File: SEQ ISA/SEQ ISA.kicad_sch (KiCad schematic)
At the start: 70 parts, among them IC1 TLX9310_TPL,F, IC2 SN74LVC4245ADW, J1 FTSH-107-01-L-DV-K-A, J2 Conn_01x02_Pin, J3 Conn_01x02_Pin, J4 Conn_01x02_Pin, J5 Conn_01x02_Pin, J6 Conn_01x02_Pin, J7 Jack-DC, J8 Conn_01x04_Pin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

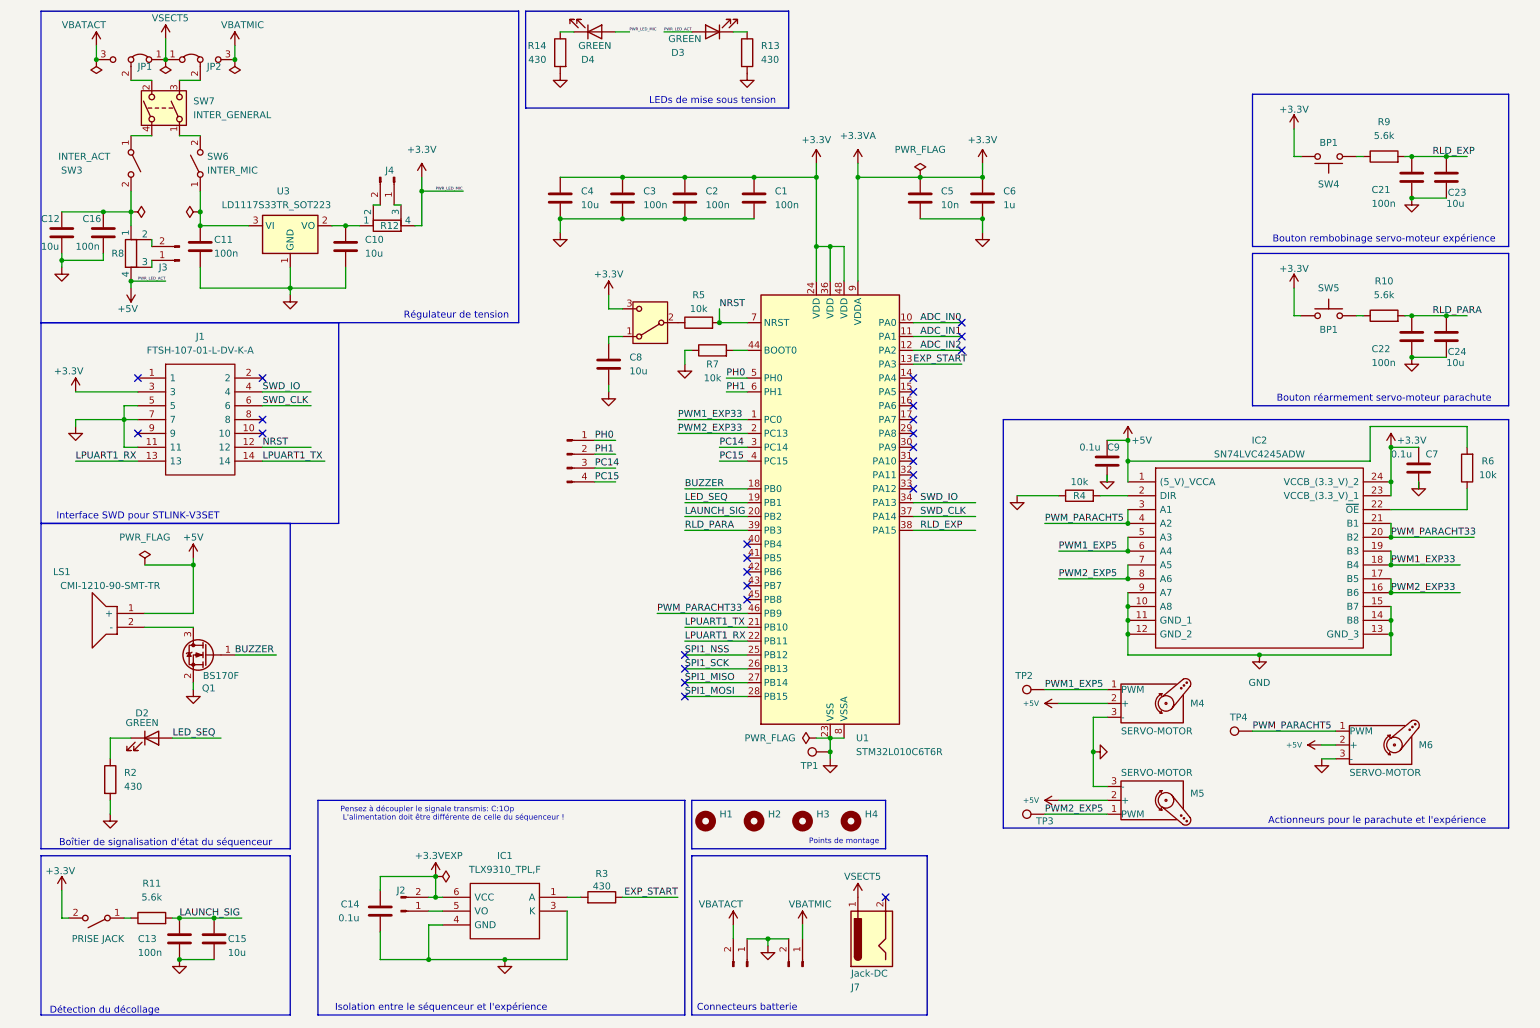
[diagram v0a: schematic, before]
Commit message: Update to KicadV9 + C movement
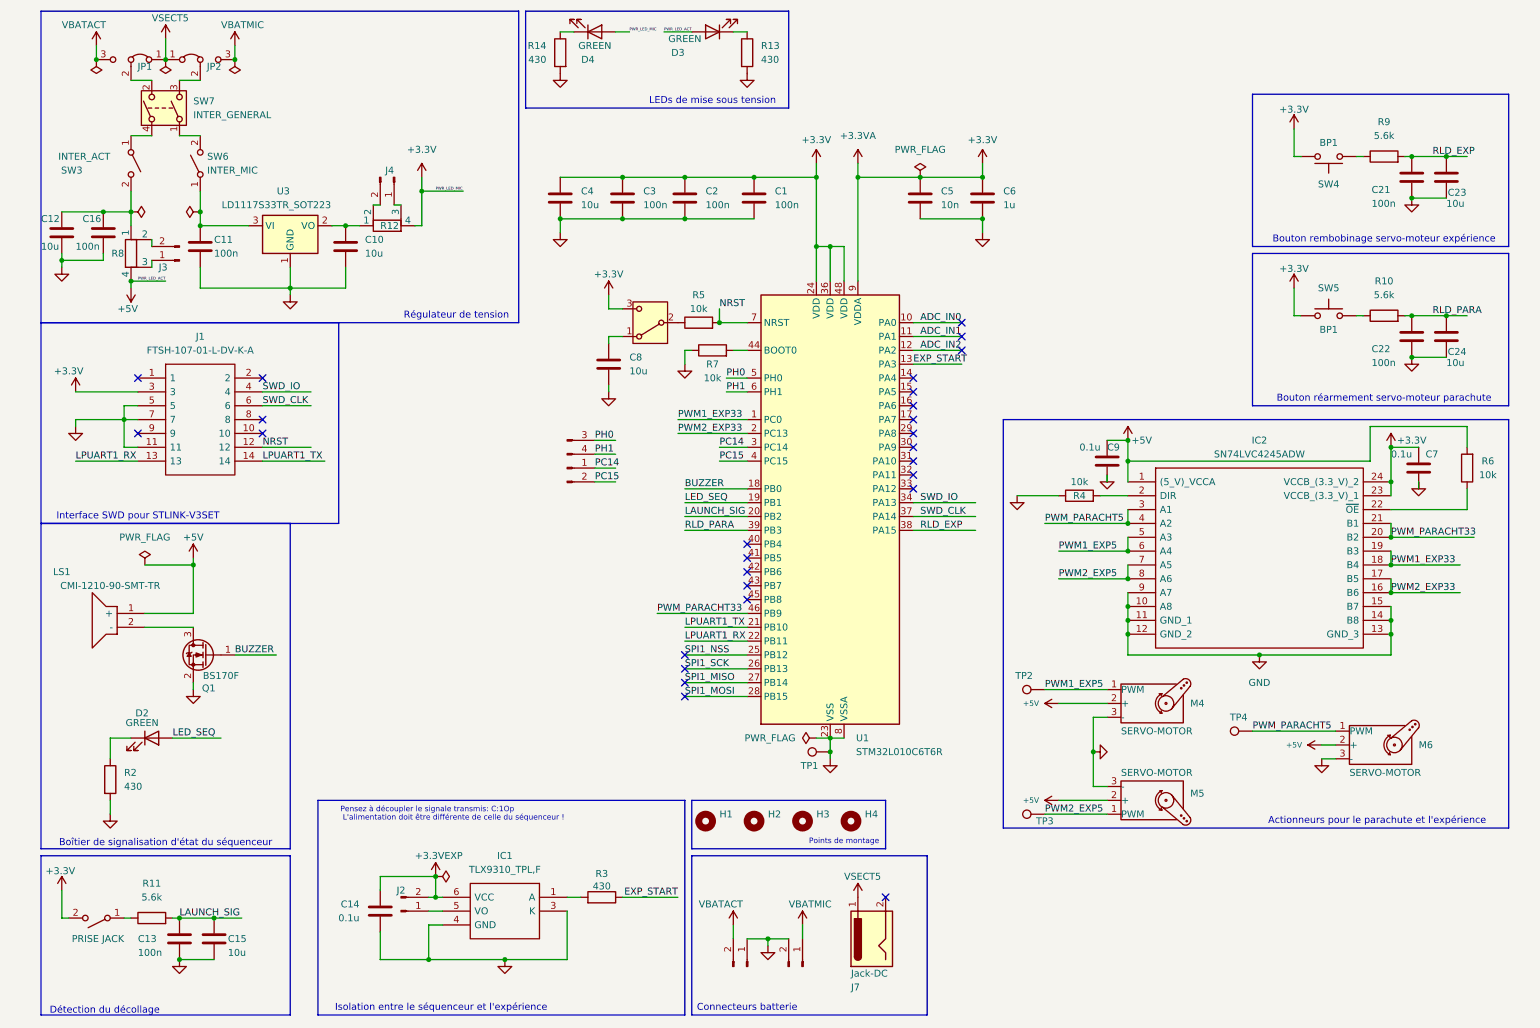
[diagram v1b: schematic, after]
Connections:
- net PC14: now also J8.1 (Pin_3); no longer J8.3 (Pin_3)
- net PC15: now also J8.2 (Pin_4); no longer J8.4 (Pin_4)
- net PH0: now also J8.3 (Pin_1); no longer J8.1 (Pin_1)
- net PH1: now also J8.4 (Pin_2); no longer J8.2 (Pin_2)
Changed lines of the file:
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@@
 (kicad_sch
-	(version 20231120)
+	(version 20250114)
 	(generator "eeschema")
-	(generator_version "8.0")
+	(generator_version "9.0")
 	(paper "A4")
 	(title_block

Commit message: Finishing PCB
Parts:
- removed C15, C24, C8: 10u, Capacitor_SMD:C_0805_2012Metric, symbol Device:C
- removed C21: 100n, Capacitor_SMD:C_0805_2012Metric, symbol Device:C
- removed R4, R5, R6: 10k, Resistor_SMD:R_0805_2012Metric, symbol Device:R
- removed R9: 5.6k, Resistor_SMD:R_0805_2012Metric, symbol Device:R
- removed SW2: SW_SPDT, Button_Switch_SMD:SW_SPDT_PCM12, symbol Switch:SW_SPDT
- removed SW4: BP1, TerminalBlock_Phoenix:TerminalBlock_Phoenix_MPT-0,5-2-2.54_1x02_P2.54mm_Horizontal, symbol Switch:SW_Push
- added R15: 5.6k, Resistor_SMD:R_0805_2012Metric, symbol Device:R
- added SW8: BP1, TerminalBlock_Phoenix:TerminalBlock_Phoenix_MPT-0,5-2-2.54_1x02_P2.54mm_Horizontal, symbol Switch:SW_Push
- C13, C22: value 100n -> 10n
- C23: value 10u -> 10n
- H1, H2, H3, H4: footprint MountingHole:MountingHole_2.2mm_M2 -> MountingHole:MountingHole_3.2mm_M3
- R13, R14, R2: value 430 -> 1k
- SW5: value BP1 -> BP2
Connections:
- net +3.3V: now also R10.1, R15.1; no longer SW5.1
- net GND: now also C23.1, IC2.2 (DIR), IC2.22 (~{OE}), J7.2, R11.1, SW5.1, SW8.2; no longer C13.2, C23.2
- net LAUNCH_SIG: now also C13.2; no longer C13.1
- net RLD_EXP: now also C23.2, R15.2, SW8.1; no longer C23.1
- net RLD_PARA: now also SW5.2
- net at SW1.1 (A): now also C13.1; no longer R11.1
- net VOLDO: now reaches C10.1, R12.1, U3.2 (VO)
- no-connect marks 27 -> 26
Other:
- moved on the sheet: C10, C13, C22, R10, R11, SW5
